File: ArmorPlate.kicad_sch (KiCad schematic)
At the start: 47 parts, among them SW1 SW_Nidec_CAS-120A1, SW2 SW_Nidec_CAS-120A1

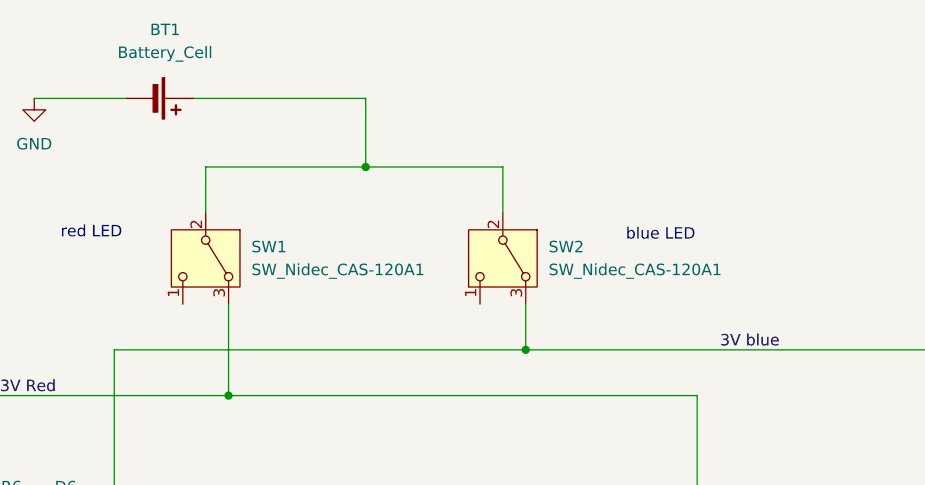
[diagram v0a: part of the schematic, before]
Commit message: updated schematic using sp3t switch
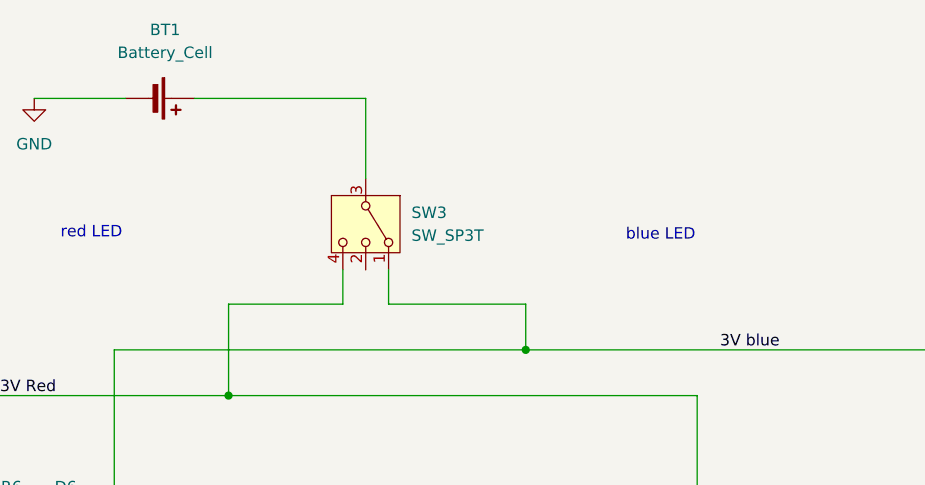
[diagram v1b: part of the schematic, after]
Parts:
- removed SW1, SW2: SW_Nidec_CAS-120A1, Button_Switch_THT:SW_Push_2P1T_Toggle_CK_PVA1xxH1xxxxxxV2, symbol Switch:SW_Nidec_CAS-120A1
- added SW3: SW_SP3T, symbol Switch:SW_SP3T
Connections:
- net 3V Red: now also SW3.4
- net 3V blue: now also SW3.1
- net at BT1.1 (+): now also SW3.3
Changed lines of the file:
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@@
 	)
 	(junction
-		(at 147.32 40.64)
-		(diameter 0)
-		(color 0 0 0 0)
-	)
-	(junction
 		(at 184.15 109.22)
 		(diameter 0)
@@
 	(wire
 		(pts
-			(xy 147.32 33.02) (xy 147.32 40.64)
+			(xy 147.32 33.02) (xy 147.32 41.91)
 		)
 		(stroke
@@
 	(wire
 		(pts
+			(xy 149.86 52.07) (xy 149.86 55.88)
+		)
+		(stroke
+			(width 0)
+			(type default)
+		)
+	)
+	(wire
+		(pts
 			(xy 86.36 95.25) (xy 86.36 107.95)
 		)
@@
 	(wire
 		(pts
+			(xy 149.86 55.88) (xy 165.1 55.88)
+		)
+		(stroke
+			(width 0)
+			(type default)
+		)
+	)
+	(wire
+		(pts
 			(xy 119.38 107.95) (xy 119.38 120.65)
 		)
@@
 	(wire
 		(pts
-			(xy 119.38 60.96) (xy 165.1 60.96)
+			(xy 144.78 55.88) (xy 132.08 55.88)
 		)
 		(stroke
@@
 	(wire
 		(pts
-			(xy 129.54 40.64) (xy 147.32 40.64)
+			(xy 119.38 60.96) (xy 165.1 60.96)
 		)
 		(stroke
@@
 	(wire
 		(pts
-			(xy 162.56 40.64) (xy 162.56 45.72)
+			(xy 201.93 109.22) (xy 201.93 121.92)
 		)
 		(stroke
@@
 	(wire
 		(pts
-			(xy 201.93 109.22) (xy 201.93 121.92)
+			(xy 144.78 52.07) (xy 144.78 55.88)
 		)
 		(stroke
@@
 	(wire
 		(pts
-			(xy 129.54 45.72) (xy 129.54 40.64)
-		)
-		(stroke
-			(width 0)
-			(type default)
-		)
-	)
-	(wire
-		(pts
-			(xy 147.32 40.64) (xy 162.56 40.64)
-		)
-		(stroke
-			(width 0)
-			(type default)
-		)
-	)
-	(wire
-		(pts
 			(xy 86.36 66.04) (xy 132.08 66.04)
 		)
@@
 	)
 	(symbol
-		(lib_id "Switch:SW_Nidec_CAS-120A1")
-		(at 129.54 50.8 270)
-		(unit 1)
-		(exclude_from_sim no)
-		(in_bom yes)
-		(on_board yes)
-		(dnp no)
-		(fields_autoplaced yes)
-		(property "Reference" "SW1"
-			(at 134.62 49.5299 90)
-			(effects
-				(font
-					(size 1.27 1.27)
-				)
-				(justify left)
-			)
-		)
-		(property "Value" "SW_Nidec_CAS-120A1"
-			(at 134.62 52.0699 90)
-			(effects
-				(font
-					(size 1.27 1.27)
-				)
-				(justify left)
-			)
-		)
-		(property "Footprint" "Button_Switch_THT:SW_Push_2P1T_Toggle_CK_PVA1xxH1xxxxxxV2"
-			(at 119.38 50.8 0)
-			(effects
-				(font
-					(size 1.27 1.27)
-				)
-				(hide yes)
-			)
-		)
-		(property "Datasheet" "https://www.nidec-components.com/e/catalog/switch/cas.pdf"
-			(at 121.92 50.8 0)
-			(effects
-				(font
-					(size 1.27 1.27)
-				)
-				(hide yes)
-			)
-		)
-		(property "Description" "Switch, single pole double throw"
-			(at 129.54 50.8 0)
-			(effects
-				(font
-					(size 1.27 1.27)
-				)
-				(hide yes)
-			)
-		)
-		(property "Mouser Part Number" "611-181D01000"
-			(at 129.54 50.8 0)
-			(effects
-				(font
-					(size 1.27 1.27)
-				)
-				(hide yes)
-			)
-		)
-		(pin "2"
-		)
-		(pin "1"
-		)
-		(pin "3"
-		)
-		(instances
-			(project "fake armor sheild 2"
-				(path "/00ff5194-078d-47e1-a4f1-0a39a16ee3f5"
-					(reference "SW1")
-					(unit 1)
-				)
-			)
-		)
-	)
-	(symbol
 		(lib_id "Device:R_US")
 		(at 107.95 107.95 90)
@@
 	)
 	(symbol
-		(lib_id "Switch:SW_Nidec_CAS-120A1")
-		(at 162.56 50.8 270)
+		(lib_id "Device:LED")
+		(at 115.57 82.55 0)
 		(unit 1)
 		(exclude_from_sim no)
@@
 		(dnp no)
 		(fields_autoplaced yes)
-		(property "Reference" "SW2"
-			(at 167.64 49.5299 90)
+		(property "Reference" "D6"
+			(at 113.9825 76.2 0)
 			(effects
 				(font
 					(size 1.27 1.27)
 				)
-				(justify left)
 			)
 		)
-		(property "Value" "SW_Nidec_CAS-120A1"
-			(at 167.64 52.0699 90)
+		(property "Value" "LED"
+			(at 113.9825 78.74 0)
 			(effects
 				(font
 					(size 1.27 1.27)
 				)
-				(justify left)
 			)
 		)
-		(property "Footprint" "Button_Switch_THT:SW_Push_2P1T_Toggle_CK_PVA1xxH1xxxxxxV2"
-			(at 152.4 50.8 0)
+		(property "Footprint" "LED_SMD:LED_0603_1608Metric_Pad1.05x0.95mm_HandSolder"
+			(at 115.57 82.55 0)
 			(effects
 				(font
@@
 			)
 		)
-		(property "Datasheet" "https://www.nidec-components.com/e/catalog/switch/cas.pdf"
-			(at 154.94 50.8 0)
+		(property "Datasheet" "~"
+			(at 115.57 82.55 0)
 			(effects
 				(font
@@
 			)
 		)
-		(property "Description" "Switch, single pole double throw"
-			(at 162.56 50.8 0)
+		(property "Description" "Light emitting diode"
+			(at 115.57 82.55 0)
 			(effects
 				(font
@@
 			)
 		)
-		(property "Mouser Part Number" "611-181D01000"
-			(at 162.56 50.8 0)
+		(property "Mouser Part Number" "710-150060SS75000"
+			(at 115.57 82.55 0)
 			(effects
 				(font
@@
 			)
 		)
-		(pin "2"
-		)
 		(pin "1"
 		)
-		(pin "3"
+		(pin "2"
 		)
 		(instances
 			(project "fake armor sheild 2"
 				(path "/00ff5194-078d-47e1-a4f1-0a39a16ee3f5"
-					(reference "SW2")
+					(reference "D6")
 					(unit 1)
 				)
@@
 	)
 	(symbol
-		(lib_id "Device:LED")
-		(at 115.57 82.55 0)
+		(lib_id "Switch:SW_SP3T")
+		(at 147.32 46.99 270)
 		(unit 1)
 		(exclude_from_sim no)
@@
 		(dnp no)
 		(fields_autoplaced yes)
-		(property "Reference" "D6"
-			(at 113.9825 76.2 0)
+		(property "Reference" "SW3"
+			(at 152.4 45.7199 90)
 			(effects
 				(font
 					(size 1.27 1.27)
 				)
+				(justify left)
 			)
 		)
-		(property "Value" "LED"
-			(at 113.9825 78.74 0)
+		(property "Value" "SW_SP3T"
+			(at 152.4 48.2599 90)
 			(effects
 				(font
 					(size 1.27 1.27)
 				)
+				(justify left)
 			)
 		)
-		(property "Footprint" "LED_SMD:LED_0603_1608Metric_Pad1.05x0.95mm_HandSolder"
-			(at 115.57 82.55 0)
+		(property "Footprint" ""
+			(at 151.765 31.115 0)
 			(effects
 				(font
@@
 		)
 		(property "Datasheet" "~"
-			(at 115.57 82.55 0)
+			(at 139.7 46.99 0)
 			(effects
 				(font
@@
 			)
 		)
-		(property "Description" "Light emitting diode"
-			(at 115.57 82.55 0)
+		(property "Description" "Switch, three position, single pole triple throw, 3 position switch, SP3T"
+			(at 147.32 46.99 0)
 			(effects
 				(font
@@
 			)
 		)
-		(property "Mouser Part Number" "710-150060SS75000"
-			(at 115.57 82.55 0)
-			(effects
-				(font
-					(size 1.27 1.27)
-				)
-				(hide yes)
-			)
-		)
-		(pin "1"
+		(pin "3"
 		)
 		(pin "2"
 		)
+		(pin "4"
+		)
+		(pin "1"
+		)
 		(instances
-			(project "fake armor sheild 2"
+			(project ""
 				(path "/00ff5194-078d-47e1-a4f1-0a39a16ee3f5"
-					(reference "D6")
+					(reference "SW3")
 					(unit 1)
 				)

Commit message: updated pcb footprint for armorplate
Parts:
- SW3: footprint (none) -> robomaster_footprints:EG1315AA
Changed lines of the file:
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@@
 			)
 		)
-		(property "Footprint" ""
+		(property "Footprint" "robomaster_footprints:EG1315AA"
 			(at 151.765 31.115 0)
 			(effects
